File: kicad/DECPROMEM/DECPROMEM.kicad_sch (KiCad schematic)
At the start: 17 parts, among them J2 JTAG, U1 CY62167, U10 DP8307, U13 74LS573, U14 74LS573, U2 CY62167, U3 ATF1508_MEM, U4 DP8307, U5 74ALS640, U6 74ALS640, U7 74LS573, U8 74ALS640, U9 DP8307, X1 40 MHz

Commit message: Updated schematic.
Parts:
- added R2: R_Small, symbol Device:R_Small
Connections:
- net BIOSEL is gone; now on net BIOSELL: U3.67 (biosel)
- net BSSXL is gone; now on net SSnL: U3.68 (bssxl)
- net D0 is gone; now on net DAL0: U1.29 (I/O0), U2.29 (I/O0), U3.5 (data_0)
- net D1 is gone; now on net DAL1: U1.31 (I/O1), U2.31 (I/O1), U3.15 (data_1)
- net D10 is gone; now on net DAL10: U1.34 (I/O10)
- net D11 is gone; now on net DAL11: U1.36 (I/O11)
- net D12 is gone; now on net DAL12: U1.39 (I/O12)
- net D13 is gone; now on net DAL13: U1.41 (I/O13)
- net D14 is gone; now on net DAL14: U1.43 (I/O14)
- net D15 is gone; now on net DAL15: U1.45 (I/O15/A20)
- net D2 is gone; now on net DAL2: U1.33 (I/O2), U2.33 (I/O2), U3.16 (data_2)
- net D3 is gone; now on net DAL3: U1.35 (I/O3), U2.35 (I/O3), U3.18 (data_3)
- net D4 is gone; now on net DAL4: U1.38 (I/O4), U2.38 (I/O4), U3.17 (data_4)
- net D5 is gone; now on net DAL5: U1.40 (I/O5), U2.40 (I/O5), U3.4 (data_5)
- net D6 is gone; now on net DAL6: U1.42 (I/O6), U2.42 (I/O6), U3.20 (data_6)
- net D7 is gone; now on net DAL7: U1.44 (I/O7), U2.44 (I/O7), U3.21 (data_7)
- net D8 is gone; now on net DAL8: U1.30 (I/O8)
- net D9 is gone; now on net DAL9: U1.32 (I/O9)
- net +5V: now also J2.4 (Pin_4), R2.1
- net GND: now also J2.10 (Pin_10), J2.2 (Pin_2)
- net MA[21..15]: now also U1.47 (~{BYTE}), U2.47 (~{BYTE}), R2.2
- net at J2.1 (Pin_1): now also U3.62 (TCK)
- net at J2.3 (Pin_3): now also U3.71 (TDO)
- net at J2.5 (Pin_5): now also U3.23 (TMS)
- net at J2.9 (Pin_9): now also U3.14 (TDI)
- no-connect marks 55 -> 59
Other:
- moved on the sheet: J2

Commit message: Updated schematic.
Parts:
- added J3: Conn_01x01_Pin, symbol Connector:Conn_01x01_Pin
- added U11: 25LCxxx, symbol Memory_EEPROM:25LCxxx
- X1: value 40 MHz -> 20 MHz
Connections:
- net +5V: now also U11.8 (VCC)
- net GND: now also U11.4 (GND)
- net MA[21..15]: now also U11.3 (~{WP})
- net at U3.73 (miso): now also U11.2 (MISO)
- net at U3.74 (ncs): now also U11.1 (~{CS})
- net at U3.75 (mosi): now also U11.5 (MOSI)
- net at U3.76 (spiclk): now also U11.6 (SCK)
- net at U3.77 (nhold): now also U11.7 (~{HOLD})
- no-connect marks 59 -> 60
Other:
- note added: "Check all pins of connector. Especially pin 33!"
- note added: "Need to add test points! A lot of them!"

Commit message: Updates to schematic.
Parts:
- added J10: BDAL08, Connector_PinHeader_2.54mm:PinHeader_1x01_P2.54mm_Vertical, symbol Connector:Conn_01x01_Pin
- added J11: BDAL09, Connector_PinHeader_2.54mm:PinHeader_1x01_P2.54mm_Vertical, symbol Connector:Conn_01x01_Pin
- added J12: BDAL10, Connector_PinHeader_2.54mm:PinHeader_1x01_P2.54mm_Vertical, symbol Connector:Conn_01x01_Pin
- added J13: BDAL11, Connector_PinHeader_2.54mm:PinHeader_1x01_P2.54mm_Vertical, symbol Connector:Conn_01x01_Pin
- added J14: BDAL12, Connector_PinHeader_2.54mm:PinHeader_1x01_P2.54mm_Vertical, symbol Connector:Conn_01x01_Pin
- added J15: BDAL13, Connector_PinHeader_2.54mm:PinHeader_1x01_P2.54mm_Vertical, symbol Connector:Conn_01x01_Pin
- added J16: BDAL14, Connector_PinHeader_2.54mm:PinHeader_1x01_P2.54mm_Vertical, symbol Connector:Conn_01x01_Pin
- added J17: BDAL15, Connector_PinHeader_2.54mm:PinHeader_1x01_P2.54mm_Vertical, symbol Connector:Conn_01x01_Pin
- added J18: BDAL16, Connector_PinHeader_2.54mm:PinHeader_1x01_P2.54mm_Vertical, symbol Connector:Conn_01x01_Pin
- added J19: BDAL17, Connector_PinHeader_2.54mm:PinHeader_1x01_P2.54mm_Vertical, symbol Connector:Conn_01x01_Pin
- added J20: BDAL18, Connector_PinHeader_2.54mm:PinHeader_1x01_P2.54mm_Vertical, symbol Connector:Conn_01x01_Pin
- added J21: BDAL19, Connector_PinHeader_2.54mm:PinHeader_1x01_P2.54mm_Vertical, symbol Connector:Conn_01x01_Pin
- added J22: BDAL20, Connector_PinHeader_2.54mm:PinHeader_1x01_P2.54mm_Vertical, symbol Connector:Conn_01x01_Pin
- added J23: BDAL21, Connector_PinHeader_2.54mm:PinHeader_1x01_P2.54mm_Vertical, symbol Connector:Conn_01x01_Pin
- added J24: BRPLYL, Connector_PinHeader_2.54mm:PinHeader_1x01_P2.54mm_Vertical, symbol Connector:Conn_01x01_Pin
- added J25: BMDENL, Connector_PinHeader_2.54mm:PinHeader_1x01_P2.54mm_Vertical, symbol Connector:Conn_01x01_Pin
- added J26: BWRITEL, Connector_PinHeader_2.54mm:PinHeader_1x01_P2.54mm_Vertical, symbol Connector:Conn_01x01_Pin
- added J27: BWLBL, Connector_PinHeader_2.54mm:PinHeader_1x01_P2.54mm_Vertical, symbol Connector:Conn_01x01_Pin
- added J28: BWHBL, Connector_PinHeader_2.54mm:PinHeader_1x01_P2.54mm_Vertical, symbol Connector:Conn_01x01_Pin
- added J29: BSDENL, Connector_PinHeader_2.54mm:PinHeader_1x01_P2.54mm_Vertical, symbol Connector:Conn_01x01_Pin
- added J3: BDAL01, Connector_PinHeader_2.54mm:PinHeader_1x01_P2.54mm_Vertical, symbol Connector:Conn_01x01_Pin
- added J30: SSnL, Connector_PinHeader_2.54mm:PinHeader_1x01_P2.54mm_Vertical, symbol Connector:Conn_01x01_Pin
- added J31: BDSL, Connector_PinHeader_2.54mm:PinHeader_1x01_P2.54mm_Vertical, symbol Connector:Conn_01x01_Pin
- added J32: BASL, Connector_PinHeader_2.54mm:PinHeader_1x01_P2.54mm_Vertical, symbol Connector:Conn_01x01_Pin
- added J33: BIOSELL, Connector_PinHeader_2.54mm:PinHeader_1x01_P2.54mm_Vertical, symbol Connector:Conn_01x01_Pin
- added J34: BDCOKH, Connector_PinHeader_2.54mm:PinHeader_1x01_P2.54mm_Vertical, symbol Connector:Conn_01x01_Pin
- added J35, J36, J37: GND, Connector_PinHeader_2.54mm:PinHeader_1x01_P2.54mm_Vertical, symbol Connector:Conn_01x01_Pin
- added J38: DAH00, Connector_PinHeader_2.54mm:PinHeader_1x01_P2.54mm_Vertical, symbol Connector:Conn_01x01_Pin
- added J39: DAH01, Connector_PinHeader_2.54mm:PinHeader_1x01_P2.54mm_Vertical, symbol Connector:Conn_01x01_Pin
- added J4: BDAL02, Connector_PinHeader_2.54mm:PinHeader_1x01_P2.54mm_Vertical, symbol Connector:Conn_01x01_Pin
- added J40: DAH02, Connector_PinHeader_2.54mm:PinHeader_1x01_P2.54mm_Vertical, symbol Connector:Conn_01x01_Pin
- added J41: DAH03, Connector_PinHeader_2.54mm:PinHeader_1x01_P2.54mm_Vertical, symbol Connector:Conn_01x01_Pin
- added J42: DAH04, Connector_PinHeader_2.54mm:PinHeader_1x01_P2.54mm_Vertical, symbol Connector:Conn_01x01_Pin
- added J43: DAH05, Connector_PinHeader_2.54mm:PinHeader_1x01_P2.54mm_Vertical, symbol Connector:Conn_01x01_Pin
- added J44: DAH06, Connector_PinHeader_2.54mm:PinHeader_1x01_P2.54mm_Vertical, symbol Connector:Conn_01x01_Pin
- added J45: DAH07, Connector_PinHeader_2.54mm:PinHeader_1x01_P2.54mm_Vertical, symbol Connector:Conn_01x01_Pin
- added J46: DAH08, Connector_PinHeader_2.54mm:PinHeader_1x01_P2.54mm_Vertical, symbol Connector:Conn_01x01_Pin
- added J47: DAH09, Connector_PinHeader_2.54mm:PinHeader_1x01_P2.54mm_Vertical, symbol Connector:Conn_01x01_Pin
- added J48: DAH10, Connector_PinHeader_2.54mm:PinHeader_1x01_P2.54mm_Vertical, symbol Connector:Conn_01x01_Pin
- added J49: DAH11, Connector_PinHeader_2.54mm:PinHeader_1x01_P2.54mm_Vertical, symbol Connector:Conn_01x01_Pin
- added J5: BDAL03, Connector_PinHeader_2.54mm:PinHeader_1x01_P2.54mm_Vertical, symbol Connector:Conn_01x01_Pin
- added J50: DAH12, Connector_PinHeader_2.54mm:PinHeader_1x01_P2.54mm_Vertical, symbol Connector:Conn_01x01_Pin
- added J51: DAH13, Connector_PinHeader_2.54mm:PinHeader_1x01_P2.54mm_Vertical, symbol Connector:Conn_01x01_Pin
- added J52: DAH14, Connector_PinHeader_2.54mm:PinHeader_1x01_P2.54mm_Vertical, symbol Connector:Conn_01x01_Pin
- added J53: DAH15, Connector_PinHeader_2.54mm:PinHeader_1x01_P2.54mm_Vertical, symbol Connector:Conn_01x01_Pin
- added J54: DAH16, Connector_PinHeader_2.54mm:PinHeader_1x01_P2.54mm_Vertical, symbol Connector:Conn_01x01_Pin
- added J55: DAH17, Connector_PinHeader_2.54mm:PinHeader_1x01_P2.54mm_Vertical, symbol Connector:Conn_01x01_Pin
- added J56: DAH18, Connector_PinHeader_2.54mm:PinHeader_1x01_P2.54mm_Vertical, symbol Connector:Conn_01x01_Pin
- added J57: DAH19, Connector_PinHeader_2.54mm:PinHeader_1x01_P2.54mm_Vertical, symbol Connector:Conn_01x01_Pin
- added J58: DAH20, Connector_PinHeader_2.54mm:PinHeader_1x01_P2.54mm_Vertical, symbol Connector:Conn_01x01_Pin
- added J59: DAH21, Connector_PinHeader_2.54mm:PinHeader_1x01_P2.54mm_Vertical, symbol Connector:Conn_01x01_Pin
- added J6: BDAL04, Connector_PinHeader_2.54mm:PinHeader_1x01_P2.54mm_Vertical, symbol Connector:Conn_01x01_Pin
- added J61: ASL, Connector_PinHeader_2.54mm:PinHeader_1x01_P2.54mm_Vertical, symbol Connector:Conn_01x01_Pin
- added J62: MDENL, Connector_PinHeader_2.54mm:PinHeader_1x01_P2.54mm_Vertical, symbol Connector:Conn_01x01_Pin
- added J63: SDENL, Connector_PinHeader_2.54mm:PinHeader_1x01_P2.54mm_Vertical, symbol Connector:Conn_01x01_Pin
- added J64: MOEL, Connector_PinHeader_2.54mm:PinHeader_1x01_P2.54mm_Vertical, symbol Connector:Conn_01x01_Pin
- added J65: MWEL, Connector_PinHeader_2.54mm:PinHeader_1x01_P2.54mm_Vertical, symbol Connector:Conn_01x01_Pin
- added J66: MCEHIGHL, Connector_PinHeader_2.54mm:PinHeader_1x01_P2.54mm_Vertical, symbol Connector:Conn_01x01_Pin
- added J67: MCELOWH, Connector_PinHeader_2.54mm:PinHeader_1x01_P2.54mm_Vertical, symbol Connector:Conn_01x01_Pin
- added J68: MLEL, Connector_PinHeader_2.54mm:PinHeader_1x01_P2.54mm_Vertical, symbol Connector:Conn_01x01_Pin
- added J69: MHEL, Connector_PinHeader_2.54mm:PinHeader_1x01_P2.54mm_Vertical, symbol Connector:Conn_01x01_Pin
- added J7: BDAL05, Connector_PinHeader_2.54mm:PinHeader_1x01_P2.54mm_Vertical, symbol Connector:Conn_01x01_Pin
- added J70: BUSDIR, Connector_PinHeader_2.54mm:PinHeader_1x01_P2.54mm_Vertical, symbol Connector:Conn_01x01_Pin
- added J71: BUSOE, Connector_PinHeader_2.54mm:PinHeader_1x01_P2.54mm_Vertical, symbol Connector:Conn_01x01_Pin
- added J72: CLK, Connector_PinHeader_2.54mm:PinHeader_1x01_P2.54mm_Vertical, symbol Connector:Conn_01x01_Pin
- added J73: MA15, Connector_PinHeader_2.54mm:PinHeader_1x01_P2.54mm_Vertical, symbol Connector:Conn_01x01_Pin
- added J74: MA16, Connector_PinHeader_2.54mm:PinHeader_1x01_P2.54mm_Vertical, symbol Connector:Conn_01x01_Pin
- added J75: MA17, Connector_PinHeader_2.54mm:PinHeader_1x01_P2.54mm_Vertical, symbol Connector:Conn_01x01_Pin
- added J76: MA18, Connector_PinHeader_2.54mm:PinHeader_1x01_P2.54mm_Vertical, symbol Connector:Conn_01x01_Pin
- added J77: MA19, Connector_PinHeader_2.54mm:PinHeader_1x01_P2.54mm_Vertical, symbol Connector:Conn_01x01_Pin
- added J78: MA20, Connector_PinHeader_2.54mm:PinHeader_1x01_P2.54mm_Vertical, symbol Connector:Conn_01x01_Pin
- added J79: MA21, Connector_PinHeader_2.54mm:PinHeader_1x01_P2.54mm_Vertical, symbol Connector:Conn_01x01_Pin
- added J8: BDAL06, Connector_PinHeader_2.54mm:PinHeader_1x01_P2.54mm_Vertical, symbol Connector:Conn_01x01_Pin
- added J80: HOLDL, Connector_PinHeader_2.54mm:PinHeader_1x01_P2.54mm_Vertical, symbol Connector:Conn_01x01_Pin
- added J81: CSL, Connector_PinHeader_2.54mm:PinHeader_1x01_P2.54mm_Vertical, symbol Connector:Conn_01x01_Pin
- added J82: SCK, Connector_PinHeader_2.54mm:PinHeader_1x01_P2.54mm_Vertical, symbol Connector:Conn_01x01_Pin
- added J83: MOSI, Connector_PinHeader_2.54mm:PinHeader_1x01_P2.54mm_Vertical, symbol Connector:Conn_01x01_Pin
- added J84: MISO, Connector_PinHeader_2.54mm:PinHeader_1x01_P2.54mm_Vertical, symbol Connector:Conn_01x01_Pin
- added J9: BDAL07, Connector_PinHeader_2.54mm:PinHeader_1x01_P2.54mm_Vertical, symbol Connector:Conn_01x01_Pin
- J2: renamed from J3; value Conn_01x01_Pin -> BDAL00; footprint (none) -> Connector_PinHeader_2.54mm:PinHeader_1x01_P2.54mm_Vertical
- J60: renamed from J2; footprint (none) -> Connector_PinHeader_2.54mm:PinHeader_2x05_P2.54mm_Vertical
- JP1: footprint (none) -> Connector_PinHeader_2.54mm:PinHeader_1x02_P2.54mm_Vertical
- R1: footprint (none) -> Resistor_THT:R_Axial_DIN0207_L6.3mm_D2.5mm_P10.16mm_Horizontal
- R2: value R_Small -> 10k; footprint (none) -> Resistor_THT:R_Axial_DIN0207_L6.3mm_D2.5mm_P10.16mm_Horizontal
- U1: renamed from U5; footprint (none) -> Package_DIP:DIP-20_W7.62mm_Socket
- U10: renamed from U11; footprint (none) -> Package_DIP:DIP-8_W7.62mm
- U11: renamed from U3; footprint (none) -> Package_LCC:PLCC-84_THT-Socket
- U12: renamed from U1; footprint (none) -> Package_SO:TSOP-I-48_18.4x12mm_P0.5mm
- U13: renamed from U2; footprint (none) -> Package_SO:TSOP-I-48_18.4x12mm_P0.5mm
- U2: renamed from U8; footprint (none) -> Package_DIP:DIP-20_W7.62mm_Socket
- U3: renamed from U10; footprint (none) -> Package_DIP:DIP-20_W7.62mm_Socket
- U4: renamed from U6; footprint (none) -> Package_DIP:DIP-20_W7.62mm_Socket
- U5: renamed from U9; footprint (none) -> Package_DIP:DIP-20_W7.62mm_Socket
- U6: renamed from U4; footprint (none) -> Package_DIP:DIP-20_W7.62mm_Socket
- U7: renamed from U13; footprint (none) -> Package_DIP:DIP-20_W7.62mm_Socket
- U8: renamed from U14; footprint (none) -> Package_DIP:DIP-20_W7.62mm_Socket
- U9: renamed from U7; footprint (none) -> Package_DIP:DIP-20_W7.62mm_Socket
- X1: footprint Oscillator:Oscillator_DIP-14 -> Package_DIP:DIP-14_W7.62mm
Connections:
- net ~{BDAL0} is gone; now on net BDAL0: J1.34 (Pin_34), U1.9 (A7), U5.8 (A7)
- net ASL: now also J61.1 (Pin_1)
- net BASL: now also J32.1 (Pin_1)
- net BDCOKH: now also J34.1 (Pin_1)
- net BDSL: now also J31.1 (Pin_1)
- net BIOSELL: now also J33.1 (Pin_1)
- net BMDENL: now also J25.1 (Pin_1)
- net BRPLYL: now also J24.1 (Pin_1)
- net BSDENL: now also J29.1 (Pin_1)
- net BWHBL: now also J28.1 (Pin_1)
- net BWLBL: now also J27.1 (Pin_1)
- net BWRITEL: now also J26.1 (Pin_1)
- net GND: now also J35.1 (Pin_1), J36.1 (Pin_1), J37.1 (Pin_1)
- net MA15: now also J73.1 (Pin_1)
- net MA16: now also J74.1 (Pin_1)
- net MA17: now also J75.1 (Pin_1)
- net MA18: now also J76.1 (Pin_1)
- net MA19: now also J77.1 (Pin_1)
- net MA20: now also J78.1 (Pin_1)
- net MA21: now also J79.1 (Pin_1)
- net MDENL: now also J62.1 (Pin_1)
- net SDENL: now also J63.1 (Pin_1)
- net SSnL: now also J30.1 (Pin_1)
- net MWEL: now reaches U11.46 (mwe), U12.11 (~{WE}), U13.11 (~{WE})
- net MWEL: now also J65.1 (Pin_1)
- net MHEL: now reaches U11.49 (mhe), U12.14 (~{BHE}), U13.14 (~{BHE})
- net MHEL: now also J69.1 (Pin_1)
- net MCELOWH: now reaches U11.45 (mcelow), U12.15 (~{BLE}), U13.15 (~{BLE})
- net MCELOWH: now also J67.1 (Pin_1)
- net MLEL: now reaches U11.22 (mle), U13.26 (~{CE1})
- net MLEL: now also J68.1 (Pin_1)
- net MOEL: now reaches U11.8 (moe), U12.28 (~{OE}), U13.28 (~{OE})
- net MOEL: now also J64.1 (Pin_1)
- net MCEHIGHL: now reaches U11.44 (nmcehigh), U12.12 (CE2)
- net MCEHIGHL: now also J66.1 (Pin_1)
- net BDAL0: now reaches J2.1 (Pin_1)
- net CLK: now reaches U11.83 (CLK), X1.8 (OUT)
- net CLK: now also J72.1 (Pin_1)
- net at U10.2 (MISO), U11.73 (miso): now also J84.1 (Pin_1)
- net CSL: now reaches U10.1 (~{CS}), U11.74 (ncs)
- net CSL: now also J81.1 (Pin_1)
- net MOSI: now reaches U10.5 (MOSI), U11.75 (mosi)
- net MOSI: now also J83.1 (Pin_1)
- net SCK: now reaches U10.6 (SCK), U11.76 (spiclk)
- net SCK: now also J82.1 (Pin_1)
- net HOLDL: now reaches U10.7 (~{HOLD}), U11.77 (nhold)
- net HOLDL: now also J80.1 (Pin_1)
- net BUSDIR renamed BUSDIRH
- net BUSDIRH: now also J70.1 (Pin_1)
- net BUSOE renamed BUSOEL
- net BUSOEL: now also J71.1 (Pin_1)
- net DAL0 renamed DAH0
- net DAH0: now also J38.1 (Pin_1)
- net DAL1 renamed DAH1
- net DAH1: now also J39.1 (Pin_1)
- net DAL10 renamed DAH10
- net DAH10: now also J48.1 (Pin_1)
- net DAL11 renamed DAH11
- net DAH11: now also J49.1 (Pin_1)
- net DAL12 renamed DAH12
- net DAH12: now also J50.1 (Pin_1)
- net DAL13 renamed DAH13
- net DAH13: now also J51.1 (Pin_1)
- net DAL14 renamed DAH14
- net DAH14: now also J52.1 (Pin_1)
- net DAL15 renamed DAH15
- net DAH15: now also J53.1 (Pin_1)
- net DAL16 renamed DAH16
- net DAH16: now also J54.1 (Pin_1)
- net DAL17 renamed DAH17
- net DAH17: now also J55.1 (Pin_1)
- net DAL18 renamed DAH18
- net DAH18: now also J56.1 (Pin_1)
- net DAL19 renamed DAH19
- net DAH19: now also J57.1 (Pin_1)
- net DAL2 renamed DAH2
- net DAH2: now also J40.1 (Pin_1)
- net DAL20 renamed DAH20
- net DAH20: now also J58.1 (Pin_1)
- net DAL21 renamed DAH21
- net DAH21: now also J59.1 (Pin_1)
- net DAL3 renamed DAH3
- net DAH3: now also J41.1 (Pin_1)
- net DAL4 renamed DAH4
- net DAH4: now also J42.1 (Pin_1)
- net DAL5 renamed DAH5
- net DAH5: now also J43.1 (Pin_1)
- net DAL6 renamed DAH6
- net DAH6: now also J44.1 (Pin_1)
- net DAL7 renamed DAH7
- net DAH7: now also J45.1 (Pin_1)
- net DAL8 renamed DAH8
- net DAH8: now also J46.1 (Pin_1)
- net DAL9 renamed DAH9
- net DAH9: now also J47.1 (Pin_1)
- net ~{BDAL10} renamed BDAL10
- net BDAL10: now also J12.1 (Pin_1)
- net ~{BDAL11} renamed BDAL11
- net BDAL11: now also J13.1 (Pin_1)
- net ~{BDAL12} renamed BDAL12
- net BDAL12: now also J14.1 (Pin_1)
- net ~{BDAL13} renamed BDAL13
- net BDAL13: now also J15.1 (Pin_1)
- net ~{BDAL14} renamed BDAL14
- net BDAL14: now also J16.1 (Pin_1)
- net ~{BDAL15} renamed BDAL15
- net BDAL15: now also J17.1 (Pin_1)
- net ~{BDAL16} renamed BDAL16
- net BDAL16: now also J18.1 (Pin_1)
- net ~{BDAL17} renamed BDAL17
- net BDAL17: now also J19.1 (Pin_1)
- net ~{BDAL18} renamed BDAL18
- net BDAL18: now also J20.1 (Pin_1)
- net ~{BDAL19} renamed BDAL19
- net BDAL19: now also J21.1 (Pin_1)
- net ~{BDAL1} renamed BDAL1
- net BDAL1: now also J3.1 (Pin_1)
- net ~{BDAL20} renamed BDAL20
- net BDAL20: now also J22.1 (Pin_1)
- net ~{BDAL21} renamed BDAL21
- net BDAL21: now also J23.1 (Pin_1)
- net ~{BDAL2} renamed BDAL2
- net BDAL2: now also J4.1 (Pin_1)
- net ~{BDAL3} renamed BDAL3
- net BDAL3: now also J5.1 (Pin_1)
- net ~{BDAL4} renamed BDAL4
- net BDAL4: now also J6.1 (Pin_1)
- net ~{BDAL5} renamed BDAL5
- net BDAL5: now also J7.1 (Pin_1)
- net ~{BDAL6} renamed BDAL6
- net BDAL6: now also J8.1 (Pin_1)
- net ~{BDAL7} renamed BDAL7
- net BDAL7: now also J9.1 (Pin_1)
- net ~{BDAL8} renamed BDAL8
- net BDAL8: now also J10.1 (Pin_1)
- net ~{BDAL9} renamed BDAL9
- net BDAL9: now also J11.1 (Pin_1)
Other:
- note removed: "Need to add test points! A lot of them!"

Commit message: Starting to do the layout.
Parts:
- added C1, C10, C11, C2, C3, C4, C5, C6, C7, C8, C9: 100n, Capacitor_THT:C_Disc_D4.3mm_W1.9mm_P5.00mm, symbol Device:C_Small
- added C12: C_Polarized_Small, Capacitor_THT:CP_Radial_Tantal_D4.5mm_P5.00mm, symbol Device:C_Polarized_Small
- added R3: 10k, Resistor_THT:R_Axial_DIN0207_L6.3mm_D2.5mm_P10.16mm_Horizontal, symbol Device:R_Small
- J1: footprint (none) -> CompLibFootprint:CTI-90
- J10, J11, J12, J13, J14, J15, J16, J17, J18, J19, J2, J20, J21, J22, J23, J24, J25, J26, J27, J28, J29, J3, J30, J31, J32, J33, J34, J35, J36, J37, J38, J39, J4, J40, J41, J42, J43, J44, J45, J46, J47, J48, J49, J5, J50, J51, J52, J53, J54, J55, J56, J57, J58, J59, J6, J61, J62, J63, J64, J65, J66, J67, J68, J69, J7, J70, J71, J72, J73, J74, J75, J76, J77, J78, J79, J8, J80, J81, J82, J83, J84, J9: footprint Connector_PinHeader_2.54mm:PinHeader_1x01_P2.54mm_Vertical -> CompLibFootprint:Testpoint
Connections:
- net +5V: now also C1.1, C10.1, C11.1, C12.1, C2.1, C3.1, C4.1, C5.1, C6.1, C7.1, C8.1, C9.1, R3.1
- net A1: now also U7.19 (Q0); no longer U7.13 (Q6)
- net A2: now also U7.18 (Q1); no longer U7.14 (Q5)
- net A3: now also U7.17 (Q2); no longer U7.15 (Q4)
- net A5: now also U7.15 (Q4); no longer U7.17 (Q2)
- net A6: now also U7.14 (Q5); no longer U7.18 (Q1)
- net A7: now also U7.13 (Q6); no longer U7.19 (Q0)
- net BDAL0: now also U1.2 (A0), U5.1 (A0); no longer U1.9 (A7), U5.8 (A7)
- net BDAL1: now also U1.3 (A1), U5.2 (A1); no longer U1.8 (A6), U5.7 (A6)
- net BDAL10: now also U3.3 (A2), U4.4 (A2); no longer U3.6 (A5), U4.7 (A5)
- net BDAL11: now also U3.4 (A3), U4.5 (A3); no longer U3.5 (A4), U4.6 (A4)
- net BDAL12: now also U3.5 (A4), U4.6 (A4); no longer U3.4 (A3), U4.5 (A3)
- net BDAL13: now also U3.6 (A5), U4.7 (A5); no longer U3.3 (A2), U4.4 (A2)
- net BDAL14: now also U3.7 (A6), U4.8 (A6); no longer U3.2 (A1), U4.3 (A1)
- net BDAL15: now also U3.8 (A7), U4.9 (A7); no longer U3.1 (A0), U4.2 (A0)
- net BDAL16: now also U2.2 (A0), U6.1 (A0); no longer U2.7 (A5), U6.6 (A5)
- net BDAL17: now also U2.3 (A1), U6.2 (A1); no longer U2.6 (A4), U6.5 (A4)
- net BDAL18: now also U2.4 (A2), U6.3 (A2); no longer U2.5 (A3), U6.4 (A3)
- net BDAL19: now also U2.5 (A3), U6.4 (A3); no longer U2.4 (A2), U6.3 (A2)
- net BDAL2: now also U1.4 (A2), U5.3 (A2); no longer U1.7 (A5), U5.6 (A5)
- net BDAL20: now also U2.6 (A4), U6.5 (A4); no longer U2.3 (A1), U6.2 (A1)
- net BDAL21: now also U2.7 (A5), U6.6 (A5); no longer U2.2 (A0), U6.1 (A0)
- net BDAL3: now also U1.5 (A3), U5.4 (A3); no longer U1.6 (A4), U5.5 (A4)
- net BDAL4: now also U1.6 (A4), U5.5 (A4); no longer U1.5 (A3), U5.4 (A3)
- net BDAL5: now also U1.7 (A5), U5.6 (A5); no longer U1.4 (A2), U5.3 (A2)
- net BDAL6: now also U1.8 (A6), U5.7 (A6); no longer U1.3 (A1), U5.2 (A1)
- net BDAL7: now also U1.9 (A7), U5.8 (A7); no longer U1.2 (A0), U5.1 (A0)
- net BDAL8: now also U3.1 (A0), U4.2 (A0); no longer U3.8 (A7), U4.9 (A7)
- net BDAL9: now also U3.2 (A1), U4.3 (A1); no longer U3.7 (A6), U4.8 (A6)
- net DAH0: now also U1.18 (B0), U5.19 (B0), U7.2 (D0); no longer U1.11 (B7), U5.12 (B7), U7.9 (D7)
- net DAH1: now also U1.17 (B1), U5.18 (B1), U7.3 (D1); no longer U1.12 (B6), U5.13 (B6), U7.8 (D6)
- net DAH10: now also U3.17 (B2), U4.16 (B2), U9.4 (D2); no longer U3.14 (B5), U4.13 (B5), U9.7 (D5)
- net DAH11: now also U3.16 (B3), U4.15 (B3), U9.5 (D3); no longer U3.15 (B4), U4.14 (B4), U9.6 (D4)
- net DAH12: now also U3.15 (B4), U4.14 (B4), U9.6 (D4); no longer U3.16 (B3), U4.15 (B3), U9.5 (D3)
- net DAH13: now also U3.14 (B5), U4.13 (B5), U9.7 (D5); no longer U3.17 (B2), U4.16 (B2), U9.4 (D2)
- net DAH14: now also U3.13 (B6), U4.12 (B6), U9.8 (D6); no longer U3.18 (B1), U4.17 (B1), U9.3 (D1)
- net DAH15: now also U3.12 (B7), U4.11 (B7), U9.9 (D7); no longer U3.19 (B0), U4.18 (B0), U9.2 (D0)
- net DAH16: now also U2.18 (B0), U6.19 (B0), U8.2 (D0); no longer U2.13 (B5), U6.14 (B5), U8.7 (D5)
- net DAH17: now also U2.17 (B1), U6.18 (B1), U8.3 (D1); no longer U2.14 (B4), U6.15 (B4), U8.6 (D4)
- net DAH18: now also U2.16 (B2), U6.17 (B2), U8.4 (D2); no longer U2.15 (B3), U6.16 (B3), U8.5 (D3)
- net DAH19: now also U2.15 (B3), U6.16 (B3), U8.5 (D3); no longer U2.16 (B2), U6.17 (B2), U8.4 (D2)
- net DAH2: now also U1.16 (B2), U5.17 (B2), U7.4 (D2); no longer U1.13 (B5), U5.14 (B5), U7.7 (D5)
- net DAH20: now also U2.14 (B4), U6.15 (B4), U8.6 (D4); no longer U2.17 (B1), U6.18 (B1), U8.3 (D1)
- net DAH21: now also U2.13 (B5), U6.14 (B5), U8.7 (D5); no longer U2.18 (B0), U6.19 (B0), U8.2 (D0)
- net DAH3: now also U1.15 (B3), U5.16 (B3), U7.5 (D3); no longer U1.14 (B4), U5.15 (B4), U7.6 (D4)
- net DAH4: now also U1.14 (B4), U5.15 (B4), U7.6 (D4); no longer U1.15 (B3), U5.16 (B3), U7.5 (D3)
- net DAH5: now also U1.13 (B5), U5.14 (B5), U7.7 (D5); no longer U1.16 (B2), U5.17 (B2), U7.4 (D2)
- net DAH6: now also U1.12 (B6), U5.13 (B6), U7.8 (D6); no longer U1.17 (B1), U5.18 (B1), U7.3 (D1)
- net DAH7: now also U1.11 (B7), U5.12 (B7), U7.9 (D7); no longer U1.18 (B0), U5.19 (B0), U7.2 (D0)
- net DAH8: now also U3.19 (B0), U4.18 (B0), U9.2 (D0); no longer U3.12 (B7), U4.11 (B7), U9.9 (D7)
- net DAH9: now also U3.18 (B1), U4.17 (B1), U9.3 (D1); no longer U3.13 (B6), U4.12 (B6), U9.8 (D6)
- net GND: now also C1.2, C10.2, C11.2, C12.2, C2.2, C3.2, C4.2, C5.2, C6.2, C7.2, C8.2, C9.2
- net MA[21..15]: no longer U10.3 (~{WP})
- new net: R3.2, U10.3 (~{WP})

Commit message: More layout done.
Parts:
- added J85: BINITL, CompLibFootprint:Testpoint, symbol Connector:Conn_01x01_Pin
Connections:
- net BINITL: now also J85.1 (Pin_1)
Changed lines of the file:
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@@
 		)
 	)
+	(wire
+		(pts
+			(xy 162.56 228.6) (xy 171.45 228.6)
+		)
+		(stroke
+			(width 0)
+			(type default)
+		)
+	)
 	(bus
 		(pts
@@
 		)
 	)
+	(label "BINITL"
+		(at 162.56 228.6 0)
+		(fields_autoplaced yes)
+		(effects
+			(font
+				(size 1.27 1.27)
+			)
+			(justify left bottom)
+		)
+	)
 	(label "DAH18"
 		(at 156.21 115.57 0)
@@
 					(unit 1)
 				)
+			)
+		)
+	)
+	(symbol
+		(lib_id "Connector:Conn_01x01_Pin")
+		(at 157.48 228.6 0)
+		(unit 1)
+		(exclude_from_sim no)
+		(in_bom yes)
+		(on_board yes)
+		(dnp no)
+		(property "Reference" "J85"
+			(at 155.194 228.346 0)
+			(effects
+				(font
+					(size 1.27 1.27)
+				)
+				(hide yes)
+			)
+		)
+		(property "Value" "BINITL"
+			(at 153.162 228.092 0)
+			(effects
+				(font
+					(size 1.27 1.27)
+				)
+			)
+		)
+		(property "Footprint" "CompLibFootprint:Testpoint"
+			(at 157.48 228.6 0)
+			(effects
+				(font
+					(size 1.27 1.27)
+				)
+				(hide yes)
+			)
+		)
+		(property "Datasheet" "~"
+			(at 157.48 228.6 0)
+			(effects
+				(font
+					(size 1.27 1.27)
+				)
+				(hide yes)
+			)
+		)
+		(property "Description" "Generic connector, single row, 01x01, script generated"
+			(at 157.48 228.6 0)
+			(effects
+				(font
+					(size 1.27 1.27)
+				)
+				(hide yes)
+			)
+		)
+		(pin "1"
+		)
+		(instances
+			(project "DECPROMEM"
+				(path "/78e01ea5-495a-4b34-a4f4-d19c2a94730d"
+					(reference "J85")
+					(unit 1)
+				)

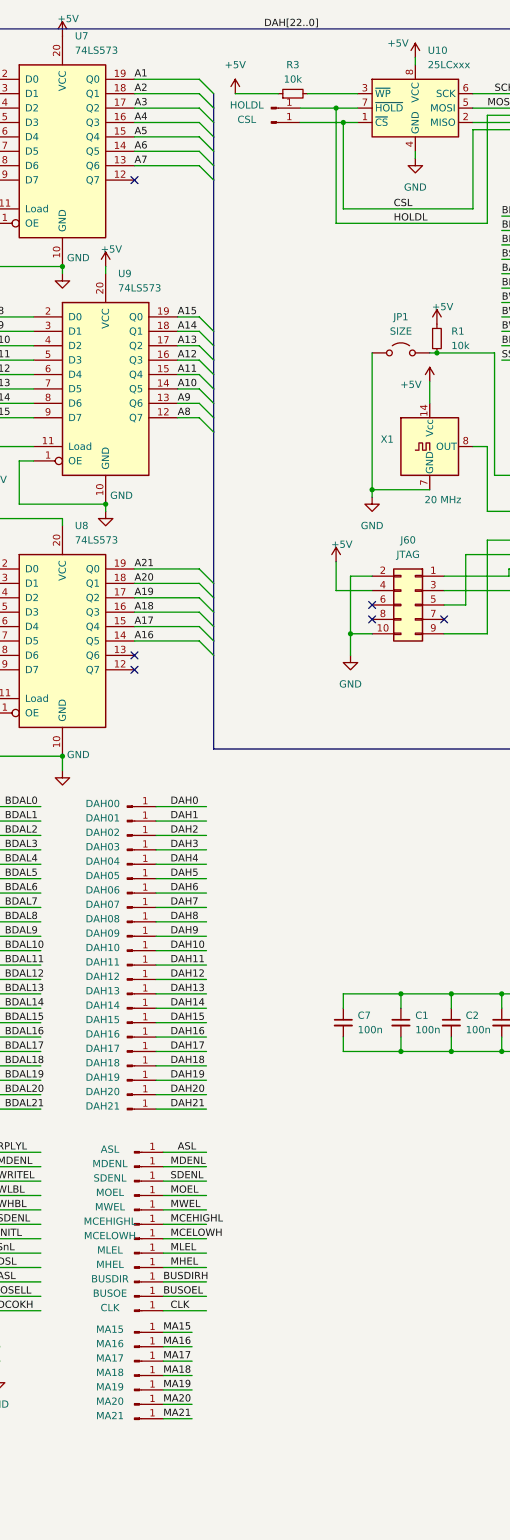
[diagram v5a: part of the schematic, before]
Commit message: Had to add more test points.
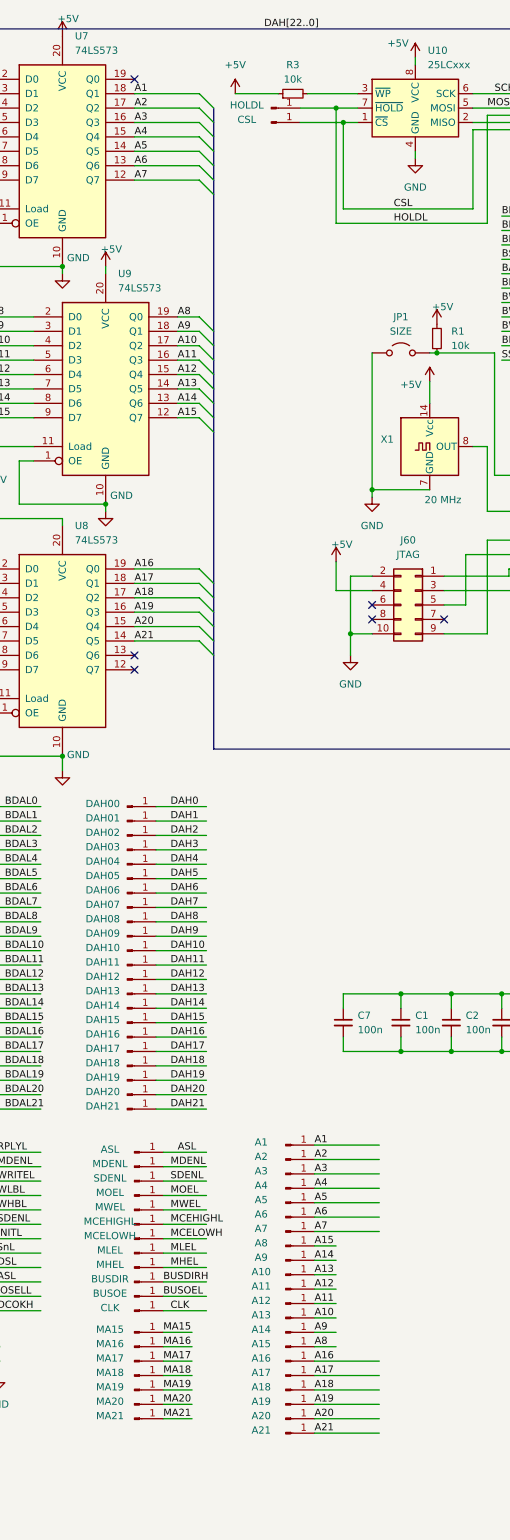
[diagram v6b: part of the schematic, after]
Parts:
- added J100: A15, CompLibFootprint:Testpoint, symbol Connector:Conn_01x01_Pin
- added J101: A16, CompLibFootprint:Testpoint, symbol Connector:Conn_01x01_Pin
- added J102: A17, CompLibFootprint:Testpoint, symbol Connector:Conn_01x01_Pin
- added J103: A18, CompLibFootprint:Testpoint, symbol Connector:Conn_01x01_Pin
- added J104: A19, CompLibFootprint:Testpoint, symbol Connector:Conn_01x01_Pin
- added J105: A20, CompLibFootprint:Testpoint, symbol Connector:Conn_01x01_Pin
- added J106: A21, CompLibFootprint:Testpoint, symbol Connector:Conn_01x01_Pin
- added J86: A1, CompLibFootprint:Testpoint, symbol Connector:Conn_01x01_Pin
- added J87: A2, CompLibFootprint:Testpoint, symbol Connector:Conn_01x01_Pin
- added J88: A3, CompLibFootprint:Testpoint, symbol Connector:Conn_01x01_Pin
- added J89: A4, CompLibFootprint:Testpoint, symbol Connector:Conn_01x01_Pin
- added J90: A5, CompLibFootprint:Testpoint, symbol Connector:Conn_01x01_Pin
- added J91: A6, CompLibFootprint:Testpoint, symbol Connector:Conn_01x01_Pin
- added J92: A7, CompLibFootprint:Testpoint, symbol Connector:Conn_01x01_Pin
- added J93: A8, CompLibFootprint:Testpoint, symbol Connector:Conn_01x01_Pin
- added J94: A9, CompLibFootprint:Testpoint, symbol Connector:Conn_01x01_Pin
- added J95: A10, CompLibFootprint:Testpoint, symbol Connector:Conn_01x01_Pin
- added J96: A11, CompLibFootprint:Testpoint, symbol Connector:Conn_01x01_Pin
- added J97: A12, CompLibFootprint:Testpoint, symbol Connector:Conn_01x01_Pin
- added J98: A13, CompLibFootprint:Testpoint, symbol Connector:Conn_01x01_Pin
- added J99: A14, CompLibFootprint:Testpoint, symbol Connector:Conn_01x01_Pin
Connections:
- net A1: now also U7.18 (Q1), J86.1 (Pin_1); no longer U7.19 (Q0)
- net A10: now also U9.17 (Q2), J98.1 (Pin_1); no longer U9.14 (Q5)
- net A11: now also U9.16 (Q3), J97.1 (Pin_1); no longer U9.15 (Q4)
- net A12: now also U9.15 (Q4), J96.1 (Pin_1); no longer U9.16 (Q3)
- net A13: now also U9.14 (Q5), J95.1 (Pin_1); no longer U9.17 (Q2)
- net A14: now also U9.13 (Q6), J94.1 (Pin_1); no longer U9.18 (Q1)
- net A15: now also U9.12 (Q7), J93.1 (Pin_1); no longer U9.19 (Q0)
- net A16: now also U8.19 (Q0), J101.1 (Pin_1); no longer U8.14 (Q5)
- net A17: now also U8.18 (Q1), J102.1 (Pin_1); no longer U8.15 (Q4)
- net A18: now also U8.17 (Q2), J103.1 (Pin_1); no longer U8.16 (Q3)
- net A19: now also U8.16 (Q3), J104.1 (Pin_1); no longer U8.17 (Q2)
- net A2: now also U7.17 (Q2), J87.1 (Pin_1); no longer U7.18 (Q1)
- net A20: now also U8.15 (Q4), J105.1 (Pin_1); no longer U8.18 (Q1)
- net A21: now also U8.14 (Q5), J106.1 (Pin_1); no longer U8.19 (Q0)
- net A3: now also U7.16 (Q3), J88.1 (Pin_1); no longer U7.17 (Q2)
- net A4: now also U7.15 (Q4), J89.1 (Pin_1); no longer U7.16 (Q3)
- net A5: now also U7.14 (Q5), J90.1 (Pin_1); no longer U7.15 (Q4)
- net A6: now also U7.13 (Q6), J91.1 (Pin_1); no longer U7.14 (Q5)
- net A7: now also U7.12 (Q7), J92.1 (Pin_1); no longer U7.13 (Q6)
- net A8: now also U9.19 (Q0), J100.1 (Pin_1); no longer U9.12 (Q7)
- net A9: now also U9.18 (Q1), J99.1 (Pin_1); no longer U9.13 (Q6)

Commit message: Added pdf file and all the gerbers
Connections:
- net A10: now also J95.1 (Pin_1); no longer J98.1 (Pin_1)
- net A11: now also J96.1 (Pin_1); no longer J97.1 (Pin_1)
- net A12: now also J97.1 (Pin_1); no longer J96.1 (Pin_1)
- net A13: now also J98.1 (Pin_1); no longer J95.1 (Pin_1)
- net A14: now also J99.1 (Pin_1); no longer J94.1 (Pin_1)
- net A15: now also J100.1 (Pin_1); no longer J93.1 (Pin_1)
- net A8: now also J93.1 (Pin_1); no longer J100.1 (Pin_1)
- net A9: now also J94.1 (Pin_1); no longer J99.1 (Pin_1)
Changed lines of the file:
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@@
 	)
 	(label "A15"
-		(at 219.71 229.87 0)
+		(at 219.71 247.65 0)
 		(fields_autoplaced yes)
 		(effects
@@
 	)
 	(label "A8"
-		(at 219.71 247.65 0)
+		(at 219.71 229.87 0)
 		(fields_autoplaced yes)
 		(effects
@@
 	)
 	(label "A14"
-		(at 219.71 232.41 0)
+		(at 219.71 245.11 0)
 		(fields_autoplaced yes)
 		(effects
@@
 	)
 	(label "A10"
-		(at 219.71 242.57 0)
+		(at 219.71 234.95 0)
 		(fields_autoplaced yes)
 		(effects
@@
 	)
 	(label "A13"
-		(at 219.71 234.95 0)
+		(at 219.71 242.57 0)
 		(fields_autoplaced yes)
 		(effects
@@
 	)
 	(label "A9"
-		(at 219.71 245.11 0)
+		(at 219.71 232.41 0)
 		(fields_autoplaced yes)
 		(effects
@@
 	)
 	(label "A12"
-		(at 219.71 237.49 0)
+		(at 219.71 240.03 0)
 		(fields_autoplaced yes)
 		(effects
@@
 	)
 	(label "A11"
-		(at 219.71 240.03 0)
-		(fields_autoplaced yes)
-		(effects
+		(at 219.71 237.49 0)
+		(fields_autoplaced yes)
+		(effects
